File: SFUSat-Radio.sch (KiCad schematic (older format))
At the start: 1 part

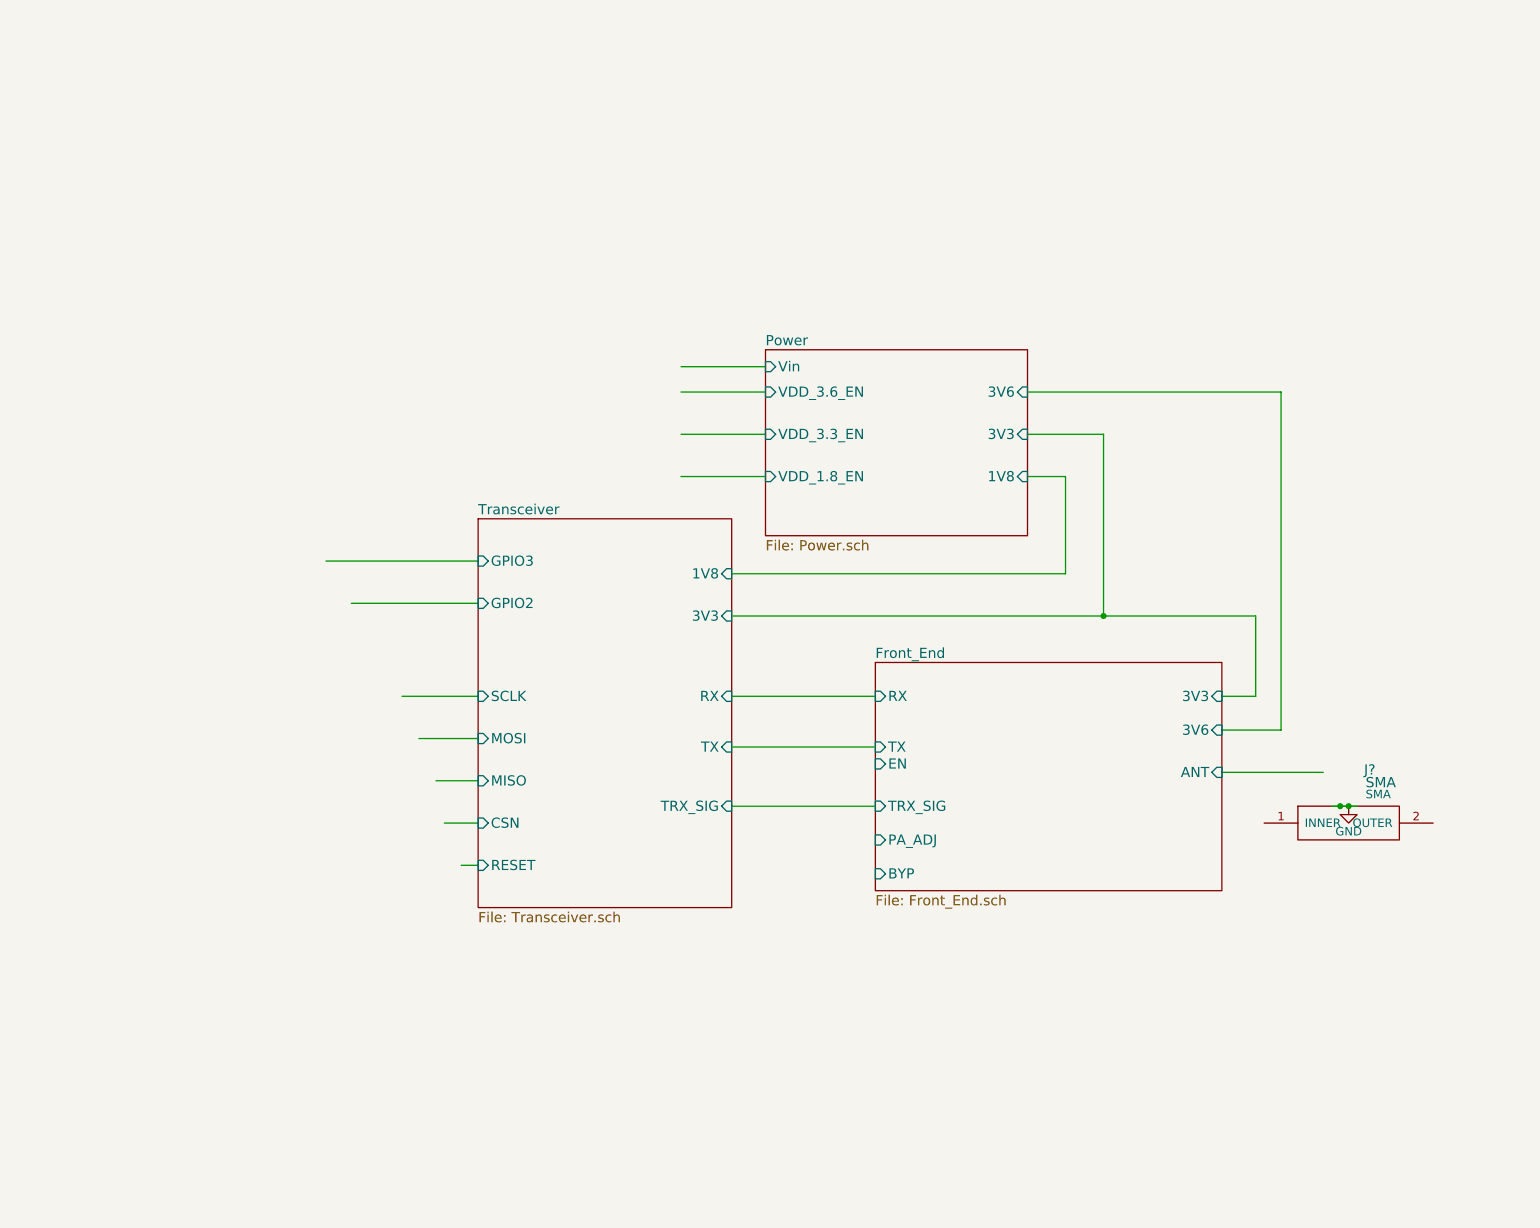
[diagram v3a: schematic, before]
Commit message: added switches for various option and nmos array to control status leds
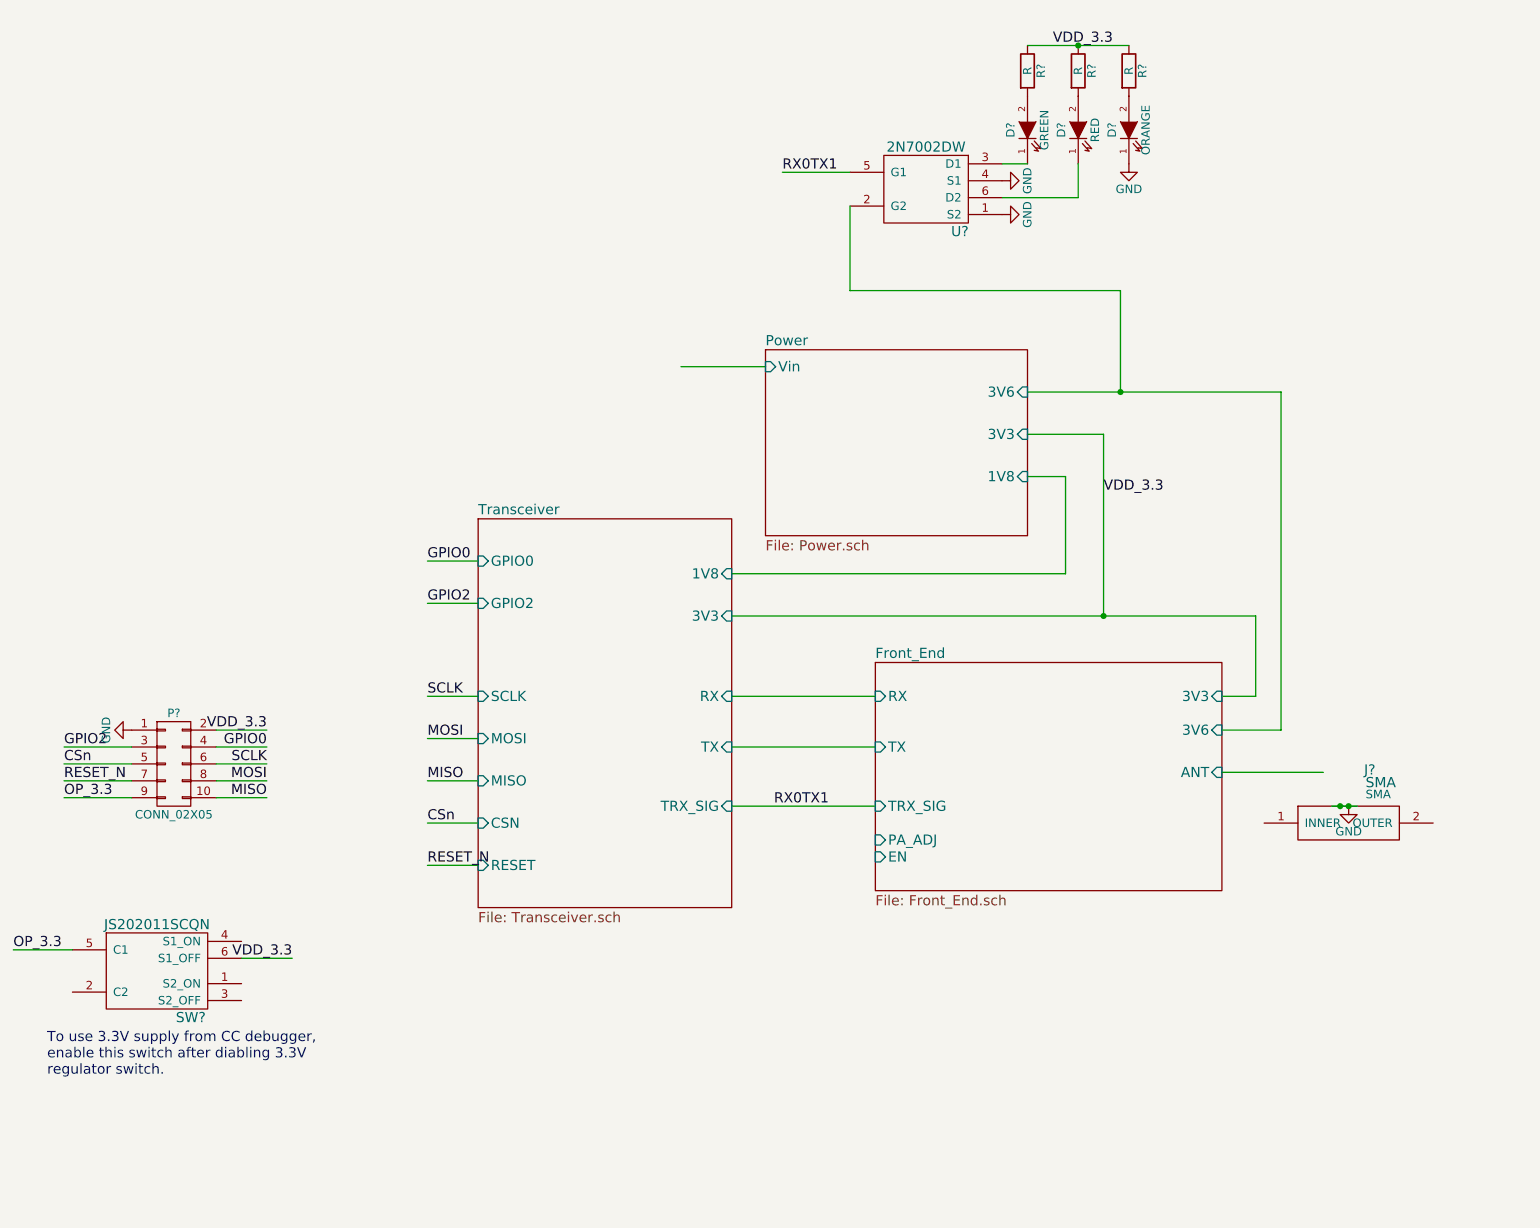
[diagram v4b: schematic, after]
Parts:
- added D?: GREEN, symbol LED
- added D?: RED, symbol LED
- added D?: ORANGE, symbol LED
- added P?: CONN_02X05, symbol CONN_02X05
- added R? (x3): R, symbol R
- added SW?: JS202011SCQN, symbol JS202011SCQN
- added U?: 2N7002DW, symbol 2N7002DW
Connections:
- net labels added: CSn, GPIO0, GPIO2, MISO, MOSI, OP_3.3, RESET_N, RX0TX1, SCLK, VDD_3.3
- wire segments 27 -> 43
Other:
- note added: "To use 3.3V supply from CC debugger, \nenable this switch after diabling 3.3V \nregulator switch."

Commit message: added a bunch of footprints and generated layout file
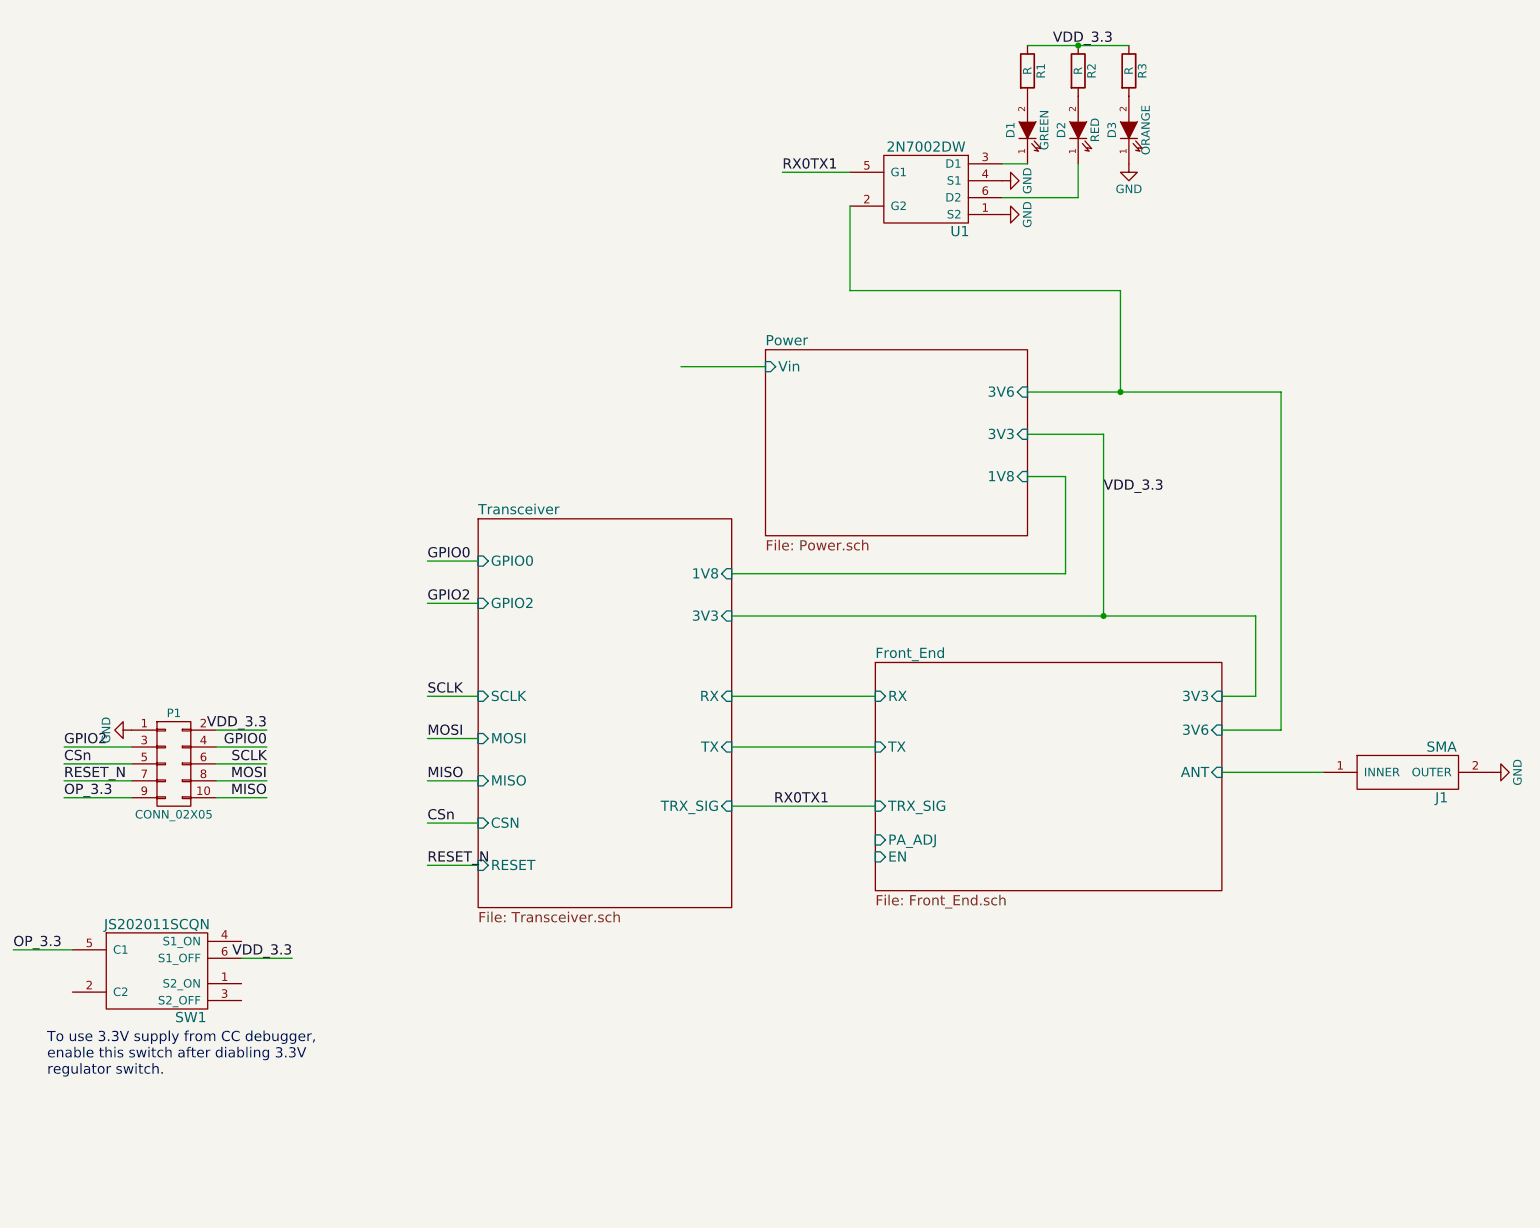
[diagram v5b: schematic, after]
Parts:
- removed J?: SMA, SMA, symbol SMA
- added J1: SMA, SFUSat-Radio:SMA_EDGE, symbol SMA
- P1: renamed from P?; footprint (none) -> Socket_Strips:Socket_Strip_Straight_2x05
- R1, R2, R3: renamed from R?; footprint (none) -> Resistors_SMD:R_0402
- SW1: renamed from SW?; footprint (none) -> SFUSat-Radio:JS2020_SMD
- U1: renamed from U?; footprint (none) -> SFUSat-Radio:SOT-363
- gave numbers to parts that had none: 3
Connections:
- wire segments 43 -> 42
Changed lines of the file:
@@
 Wire Wire Line
 	8100 5050 8700 5050
-$Comp
-L SMA J?
-U 1 1 58210E85
-P 8850 5350
-F 0 "J?" H 8975 5665 60  0000 C CNN
-F 1 "SMA" H 9040 5590 60  0000 C CNN
-F 2 "SMA" H 9025 5520 50  0000 C CNN
-F 3 "" H 8850 5350 60  0000 C CNN
-	1    8850 5350
-	1    0    0    -1
-$EndComp
-$Comp
-L GND #PWR01
-U 1 1 58212D02
-P 8850 5250
-F 0 "#PWR01" H 8850 5000 50  0001 C CNN
-F 1 "GND" H 8850 5100 50  0000 C CNN
-F 2 "" H 8850 5250 50  0000 C CNN
-F 3 "" H 8850 5250 50  0000 C CNN
-	1    8850 5250
-	1    0    0    -1
-$EndComp
-Wire Wire Line
-	8750 5250 8900 5250
-Connection ~ 8800 5250
-Connection ~ 8850 5250
 Wire Wire Line
 	5200 4600 6050 4600
@@
 	5400 2650 4900 2650
 $Comp
-L CONN_02X05 P?
+L CONN_02X05 P1
 U 1 1 587CD1D3
 P 1900 5000
-F 0 "P?" H 1900 5300 50  0000 C CNN
+F 0 "P1" H 1900 5300 50  0000 C CNN
 F 1 "CONN_02X05" H 1900 4700 50  0000 C CNN
-F 2 "" H 1900 3800 50  0000 C CNN
+F 2 "Socket_Strips:Socket_Strip_Straight_2x05" H 1900 3800 50  0001 C CNN
 F 3 "" H 1900 3800 50  0000 C CNN
 	1    1900 5000
@@
 $EndComp
 $Comp
-L GND #PWR?
+L GND #PWR01
 U 1 1 587CE076
 P 1650 4800
-F 0 "#PWR?" H 1650 4550 50  0001 C CNN
+F 0 "#PWR01" H 1650 4550 50  0001 C CNN
 F 1 "GND" H 1650 4650 50  0000 C CNN
 F 2 "" H 1650 4800 50  0000 C CNN
@@
 VDD_3.3
 $Comp
-L JS202011SCQN SW?
+L JS202011SCQN SW1
 U 1 1 587DE706
 P 1800 6100
-F 0 "SW?" H 2000 5700 60  0000 C CNN
+F 0 "SW1" H 2000 5700 60  0000 C CNN
 F 1 "JS202011SCQN" H 1800 6250 60  0000 C CNN
-F 2 "" H 1800 6100 60  0000 C CNN
+F 2 "SFUSat-Radio:JS2020_SMD" H 1800 6100 60  0001 C CNN
 F 3 "" H 1800 6100 60  0000 C CNN
 	1    1800 6100
@@
 To use 3.3V supply from CC debugger, \nenable this switch after diabling 3.3V \nregulator switch.
 $Comp
-L 2N7002DW U?
+L 2N7002DW U1
 U 1 1 587E8AE8
 P 6350 1600
-F 0 "U?" H 6550 1350 60  0000 C CNN
+F 0 "U1" H 6550 1350 60  0000 C CNN
 F 1 "2N7002DW" H 6350 1850 60  0000 C CNN
-F 2 "" H 6350 1600 60  0000 C CNN
+F 2 "SFUSat-Radio:SOT-363" H 6350 1600 60  0001 C CNN
 F 3 "" H 6350 1600 60  0000 C CNN
 	1    6350 1600
@@
 $EndComp
 $Comp
-L LED D?
+L LED D1
 U 1 1 587E94F9
 P 6950 1250
-F 0 "D?" H 6950 1350 50  0000 C CNN
+F 0 "D1" H 6950 1350 50  0000 C CNN
 F 1 "GREEN" H 6950 1150 50  0000 C CNN
-F 2 "" H 6950 1250 50  0000 C CNN
+F 2 "" H 6950 1250 50  0001 C CNN
 F 3 "" H 6950 1250 50  0000 C CNN
 	1    6950 1250
@@
 $EndComp
 $Comp
-L R R?
+L R R1
 U 1 1 587EAD14
 P 6950 900
-F 0 "R?" V 7030 900 50  0000 C CNN
+F 0 "R1" V 7030 900 50  0000 C CNN
 F 1 "R" V 6950 900 50  0000 C CNN
-F 2 "" V 6880 900 50  0000 C CNN
+F 2 "Resistors_SMD:R_0402" V 6880 900 50  0001 C CNN
 F 3 "" H 6950 900 50  0000 C CNN
 	1    6950 900
@@
 $EndComp
 $Comp
-L R R?
+L R R2
 U 1 1 587EC56D
 P 7250 900
-F 0 "R?" V 7330 900 50  0000 C CNN
+F 0 "R2" V 7330 900 50  0000 C CNN
 F 1 "R" V 7250 900 50  0000 C CNN
-F 2 "" V 7180 900 50  0000 C CNN
+F 2 "Resistors_SMD:R_0402" V 7180 900 50  0001 C CNN
 F 3 "" H 7250 900 50  0000 C CNN
 	1    7250 900
@@
 $EndComp
 $Comp
-L LED D?
+L LED D2
 U 1 1 587EC634
 P 7250 1250
-F 0 "D?" H 7250 1350 50  0000 C CNN
+F 0 "D2" H 7250 1350 50  0000 C CNN
 F 1 "RED" H 7250 1150 50  0000 C CNN
-F 2 "" H 7250 1250 50  0000 C CNN
+F 2 "" H 7250 1250 50  0001 C CNN
 F 3 "" H 7250 1250 50  0000 C CNN
 	1    7250 1250
@@
 $EndComp
 $Comp
-L GND #PWR?
+L GND #PWR02
 U 1 1 587EE6E2
 P 6800 1550
-F 0 "#PWR?" H 6800 1300 50  0001 C CNN
+F 0 "#PWR02" H 6800 1300 50  0001 C CNN
 F 1 "GND" H 6800 1400 50  0000 C CNN
 F 2 "" H 6800 1550 50  0000 C CNN
@@
 $EndComp
 $Comp
-L GND #PWR?
+L GND #PWR03
 U 1 1 587EE79C
 P 6800 1750
-F 0 "#PWR?" H 6800 1500 50  0001 C CNN
+F 0 "#PWR03" H 6800 1500 50  0001 C CNN
 F 1 "GND" H 6800 1600 50  0000 C CNN
 F 2 "" H 6800 1750 50  0000 C CNN
@@
 	7250 1650 7250 1450
 $Comp
-L LED D?
+L LED D3
 U 1 1 587F1822
 P 7550 1250
-F 0 "D?" H 7550 1350 50  0000 C CNN
+F 0 "D3" H 7550 1350 50  0000 C CNN
 F 1 "ORANGE" H 7550 1150 50  0000 C CNN
-F 2 "" H 7550 1250 50  0000 C CNN
+F 2 "" H 7550 1250 50  0001 C CNN
 F 3 "" H 7550 1250 50  0000 C CNN
 	1    7550 1250
@@
 $EndComp
 $Comp
-L R R?
+L R R3
 U 1 1 587F1910
 P 7550 900
-F 0 "R?" V 7630 900 50  0000 C CNN
+F 0 "R3" V 7630 900 50  0000 C CNN
 F 1 "R" V 7550 900 50  0000 C CNN
-F 2 "" V 7480 900 50  0000 C CNN
+F 2 "Resistors_SMD:R_0402" V 7480 900 50  0001 C CNN
 F 3 "" H 7550 900 50  0000 C CNN
 	1    7550 900
@@
 $EndComp
 $Comp
-L GND #PWR?
+L GND #PWR04
 U 1 1 587F1A5F
 P 7550 1450
-F 0 "#PWR?" H 7550 1200 50  0001 C CNN
+F 0 "#PWR04" H 7550 1200 50  0001 C CNN
 F 1 "GND" H 7550 1300 50  0000 C CNN
 F 2 "" H 7550 1450 50  0000 C CNN
@@
 Text Label 950  6100 0    60   ~ 0
 OP_3.3
+$Comp
+L SMA J1
+U 1 1 5883A1B6
+P 9200 5050
+F 0 "J1" H 9400 4900 60  0000 C CNN
+F 1 "SMA" H 9400 5200 60  0000 C CNN
+F 2 "SFUSat-Radio:SMA_EDGE" H 9200 5050 60  0001 C CNN
+F 3 "" H 9200 5050 60  0000 C CNN
+	1    9200 5050
+	1    0    0    -1
+$EndComp
+$Comp
+L GND #PWR05
+U 1 1 5883A521
+P 9700 5050
+F 0 "#PWR05" H 9700 4800 50  0001 C CNN
+F 1 "GND" H 9700 4900 50  0000 C CNN
+F 2 "" H 9700 5050 50  0000 C CNN
+F 3 "" H 9700 5050 50  0000 C CNN
+	1    9700 5050
+	0    -1   -1   0
+$EndComp
 $EndSCHEMATC

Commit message: setup netclasses and added more footprints
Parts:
- D1, D2, D3: footprint (none) -> SFUSat-Radio:LED_0603
- SW1: footprint SFUSat-Radio:JS2020_SMD -> SFUSat-Radio:JS2020_TH
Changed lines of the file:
@@
 F 0 "SW1" H 2000 5700 60  0000 C CNN
 F 1 "JS202011SCQN" H 1800 6250 60  0000 C CNN
-F 2 "SFUSat-Radio:JS2020_SMD" H 1800 6100 60  0001 C CNN
+F 2 "SFUSat-Radio:JS2020_TH" H 1800 6100 60  0001 C CNN
 F 3 "" H 1800 6100 60  0000 C CNN
 	1    1800 6100
@@
 F 0 "D1" H 6950 1350 50  0000 C CNN
 F 1 "GREEN" H 6950 1150 50  0000 C CNN
-F 2 "" H 6950 1250 50  0001 C CNN
+F 2 "SFUSat-Radio:LED_0603" H 6950 1250 50  0001 C CNN
 F 3 "" H 6950 1250 50  0000 C CNN
 	1    6950 1250
@@
 F 0 "D2" H 7250 1350 50  0000 C CNN
 F 1 "RED" H 7250 1150 50  0000 C CNN
-F 2 "" H 7250 1250 50  0001 C CNN
+F 2 "SFUSat-Radio:LED_0603" H 7250 1250 50  0001 C CNN
 F 3 "" H 7250 1250 50  0000 C CNN
 	1    7250 1250
@@
 F 0 "D3" H 7550 1350 50  0000 C CNN
 F 1 "ORANGE" H 7550 1150 50  0000 C CNN
-F 2 "" H 7550 1250 50  0001 C CNN
+F 2 "SFUSat-Radio:LED_0603" H 7550 1250 50  0001 C CNN
 F 3 "" H 7550 1250 50  0000 C CNN
 	1    7550 1250
